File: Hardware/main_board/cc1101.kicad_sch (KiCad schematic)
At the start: 50 parts, among them T1 B0310J50100AHF, U10 BGS13S4N9E6327XTSA1, U8 CC1101RGP, U9 BGS13S4N9E6327XTSA1, Y3 26MHz

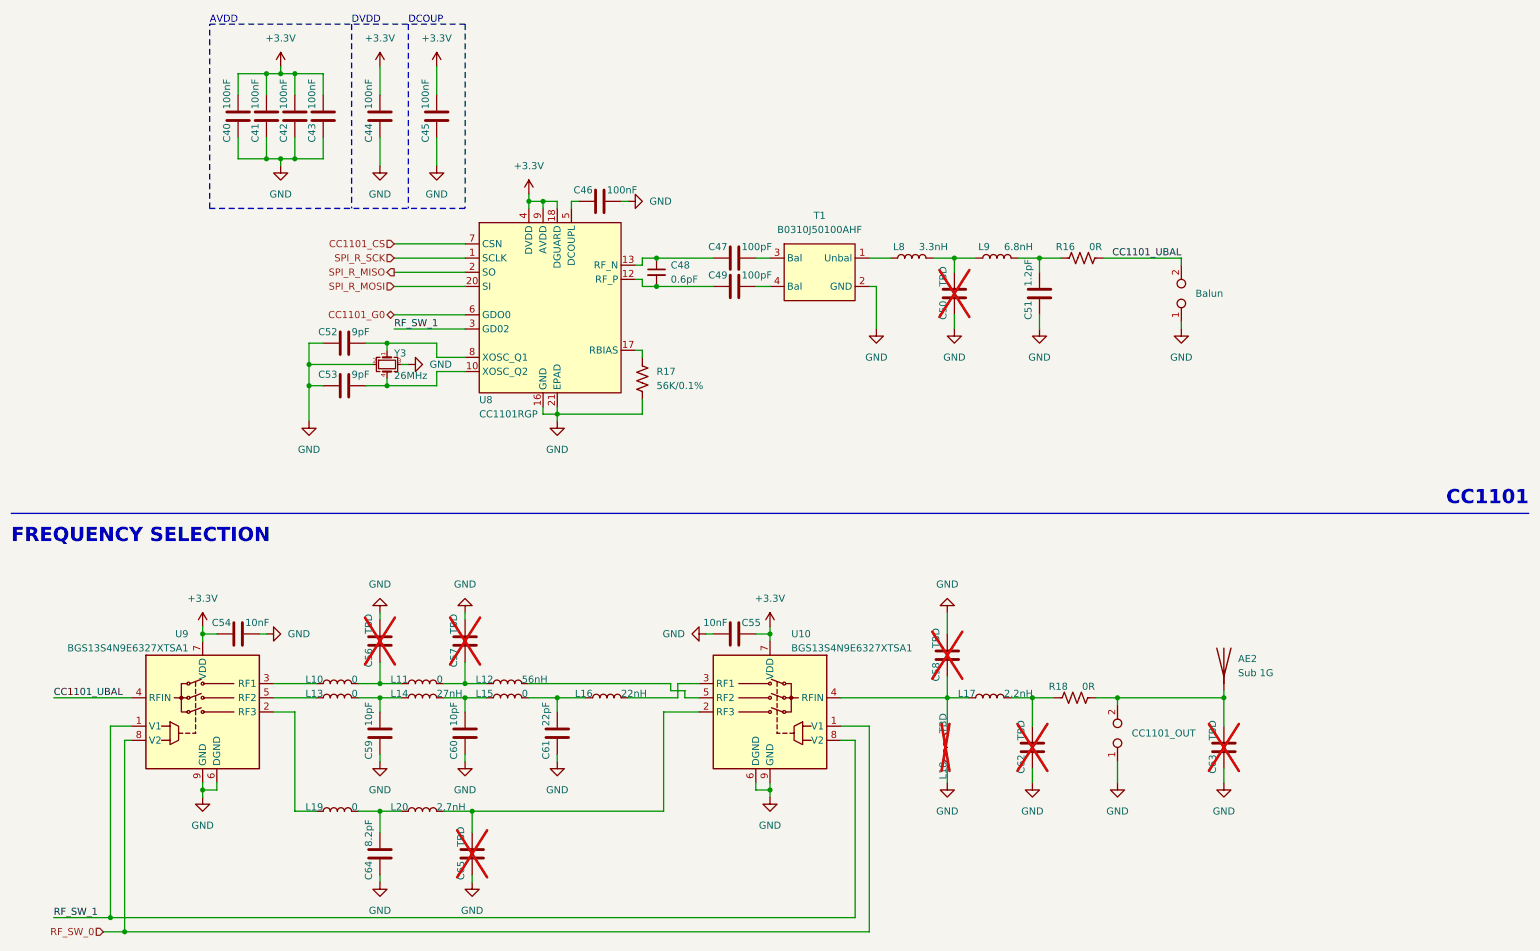
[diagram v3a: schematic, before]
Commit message: layout: change some of the footprint and start to layout
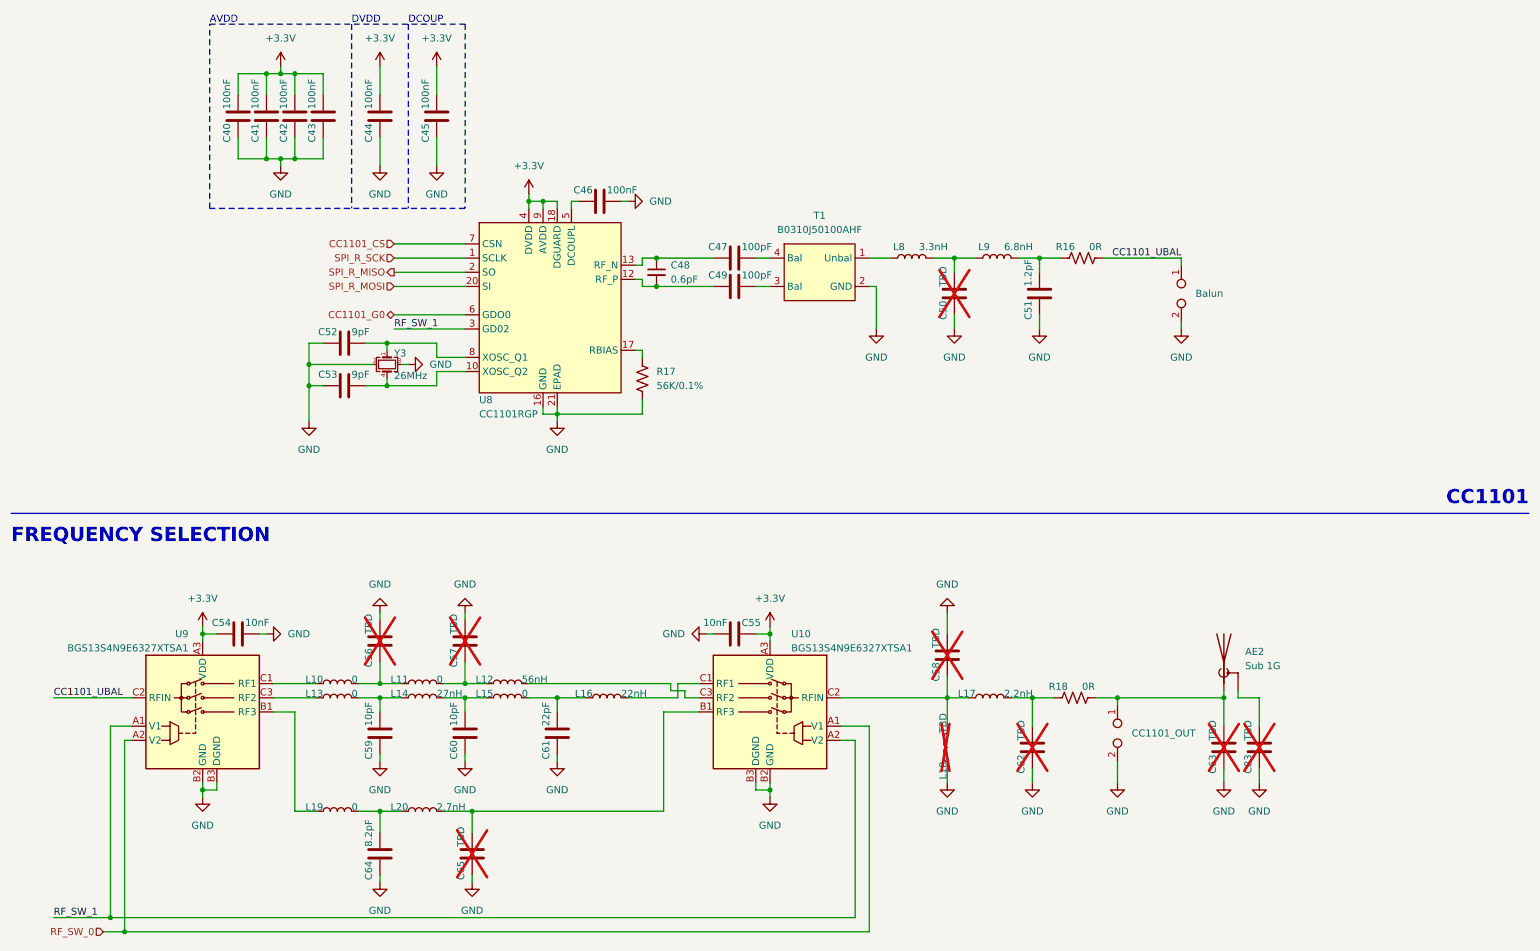
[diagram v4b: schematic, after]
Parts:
- added C83: TBD, Capacitor_SMD:C_0402_1005Metric, symbol Device:C
- AE2: footprint (none) -> Library:ANT_SUB1G; symbol Device:Antenna -> Device:Antenna_Shield
- C47, C48, C49, C50, C51, C56, C57, C59, C60, C61, C64, C65: footprint Capacitor_SMD:C_0402_1005Metric -> Capacitor_SMD:C_0201_0603Metric
- L10, L11, L12, L13, L14, L15, L16, L19, L20, L8, L9: footprint Inductor_SMD:L_0402_1005Metric -> Inductor_SMD:L_0201_0603Metric
- L18: footprint nductor_SMD:L_0402_1005Metric -> Inductor_SMD:L_0402_1005Metric
- R16: footprint Resistor_SMD:R_0402_1005Metric -> Resistor_SMD:R_0201_0603Metric
- T1: footprint (none) -> Library:B0310J50100AHF
- TP32, TP33: footprint TestPoint:TestPoint_2Pads_Pitch2.54mm_Drill0.8mm -> Connector_Coaxial:U.FL_Molex_MCRF_73412-0110_Vertical
- U10, U9: footprint (none) -> Library:BGA-9_3x3_1.2x1.2mm
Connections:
- net +3.3V: now also U10.A3 (VDD), U9.A3 (VDD); no longer U10.7 (VDD), U9.7 (VDD)
- net CC1101_UBAL: now also TP32.1, U9.C2 (RFIN); no longer TP32.2, U9.4 (RFIN)
- net GND: now also TP32.2, TP33.2, U10.B2 (GND), U10.B3 (DGND), U9.B2 (GND), U9.B3 (DGND), C83.1; no longer TP32.1, TP33.1, U10.6 (DGND), U10.9 (GND), U9.6 (DGND), U9.9 (GND)
- net RF_SW_0: now also U10.A1 (V1), U9.A2 (V2); no longer U10.1 (V1), U9.8 (V2)
- net RF_SW_1: now also U10.A2 (V2), U9.A1 (V1); no longer U10.8 (V2), U9.1 (V1)
- net at C49.2: now also T1.3 (Bal); no longer T1.4 (Bal)
- net at C65.2, L20.2: now also U10.B1 (RF3); no longer U10.2 (RF3)
- net at L16.2: now also U10.C1 (RF1); no longer U10.3 (RF1)
- net at C58.1, L17.1, L18.2: now also U10.C2 (RFIN); no longer U10.4 (RFIN)
- net at L12.2: now also U10.C3 (RF2); no longer U10.5 (RF2)
- net at L10.1: now also U9.C1 (RF1); no longer U9.3 (RF1)
- net at AE2.1 (A), C63.2, R18.2: now also TP33.1; no longer TP33.2
- net at L19.1: now also U9.B1 (RF3); no longer U9.2 (RF3)
- net at C47.2: now also T1.4 (Bal); no longer T1.3 (Bal)
- net at L13.1: now also U9.C3 (RF2); no longer U9.5 (RF2)
- new net: AE2.2 (Shield), C83.2

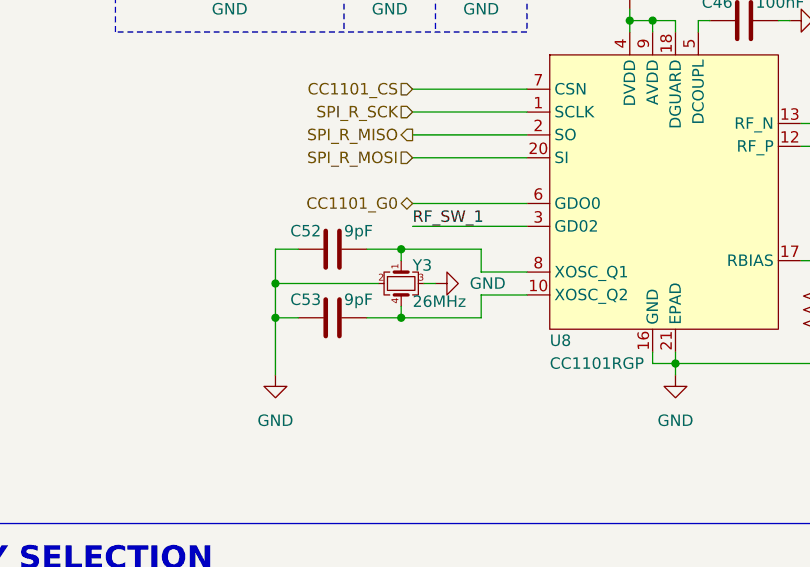
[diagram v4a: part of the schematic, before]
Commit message: layout: finish the Sub-1G filter
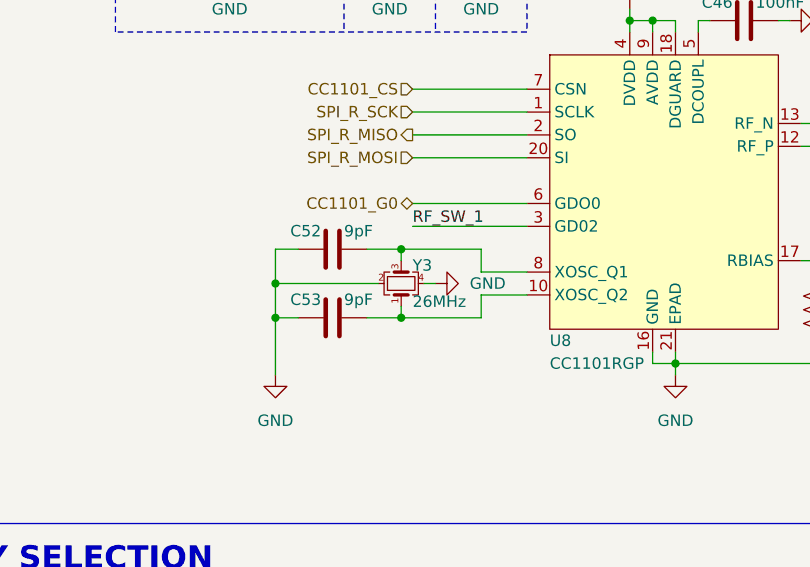
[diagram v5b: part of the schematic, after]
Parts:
- Y3: symbol Device:Crystal_GND23_Small -> Device:Crystal_GND24_Small
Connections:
- net GND: now also Y3.4; no longer Y3.3
- net at C53.2, U8.10 (XOSC_Q2): now also Y3.1; no longer Y3.4
- net at C52.2, U8.8 (XOSC_Q1): now also Y3.3; no longer Y3.1
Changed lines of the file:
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@@
 	)
 	(symbol
-		(lib_id "Device:Crystal_GND23_Small")
+		(lib_id "Device:Crystal_GND24_Small")
 		(at 80.01 81.28 270)
+		(mirror x)
 		(unit 1)
 		(exclude_from_sim no)
@@
 					(size 1.27 1.27)
 				)
-				(justify left bottom)
+				(justify left top)
 			)
 		)
@@
 					(size 1.27 1.27)
 				)
-				(justify left top)
+				(justify left bottom)
 			)
 		)
@@
 			)
 		)
-		(property "Description" "Four pin crystal, GND on pins 2 and 3, small symbol"
+		(property "Description" "Four pin crystal, GND on pins 2 and 4, small symbol"
 			(at 80.01 81.28 0)
 			(effects

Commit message: layout: optimise cc1101 and start the stm32
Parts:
- TP32, TP33: footprint Connector_Coaxial:U.FL_Molex_MCRF_73412-0110_Vertical -> Library:TP_DP
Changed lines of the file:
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@@
 			)
 		)
-		(property "Footprint" "Connector_Coaxial:U.FL_Molex_MCRF_73412-0110_Vertical"
+		(property "Footprint" "Library:TP_DP"
 			(at 210.82 147.32 0)
 			(effects
@@
 			)
 		)
-		(property "Footprint" "Connector_Coaxial:U.FL_Molex_MCRF_73412-0110_Vertical"
+		(property "Footprint" "Library:TP_DP"
 			(at 222.25 68.58 0)
 			(effects
